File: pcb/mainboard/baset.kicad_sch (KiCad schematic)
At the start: 63 parts, among them J27 0826-1G1T-23-F, U33 ECS-1612MV-250-CN, U34 KSZ9031RN, U35 RCLAMP0514M, U36 RCLAMP0514M, U8 XC7K70T-2FBG484C

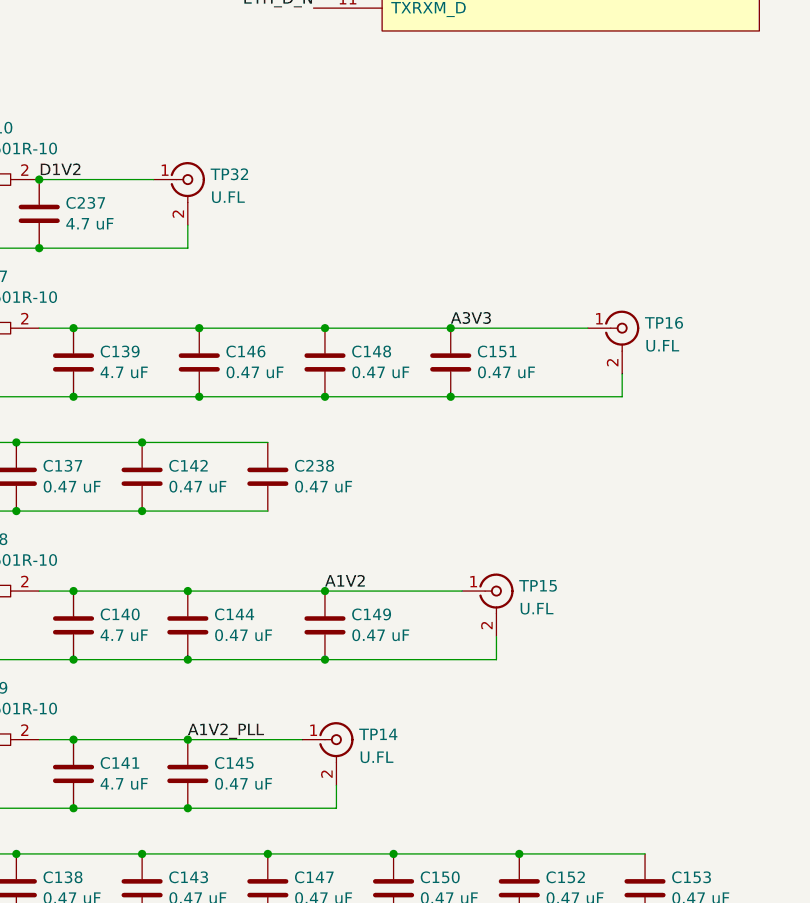
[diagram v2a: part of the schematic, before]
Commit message: Updated schematic with some notes on rework
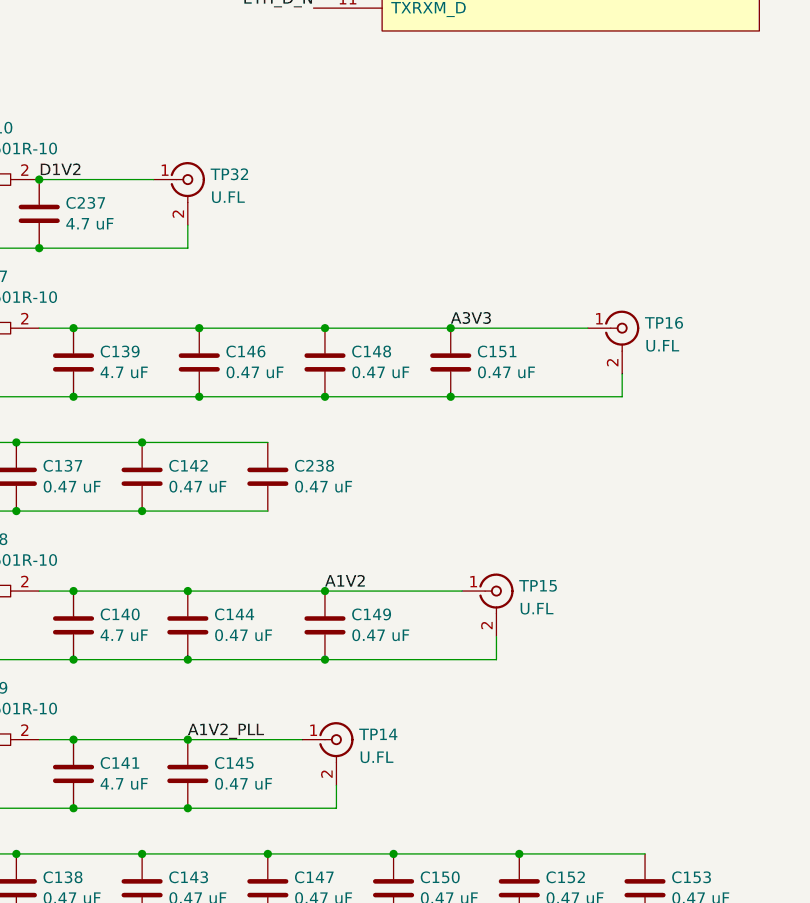
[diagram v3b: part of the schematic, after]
